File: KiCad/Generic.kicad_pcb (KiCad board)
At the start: 2 copper layers, 19 x 29 mm, 16 parts, among them J1 Connector, J2 USB-C, J3 VBUS, M1 D24V5F3-NoSHDN, U1 ESP32-WROOM-32, U2 FT231XQ

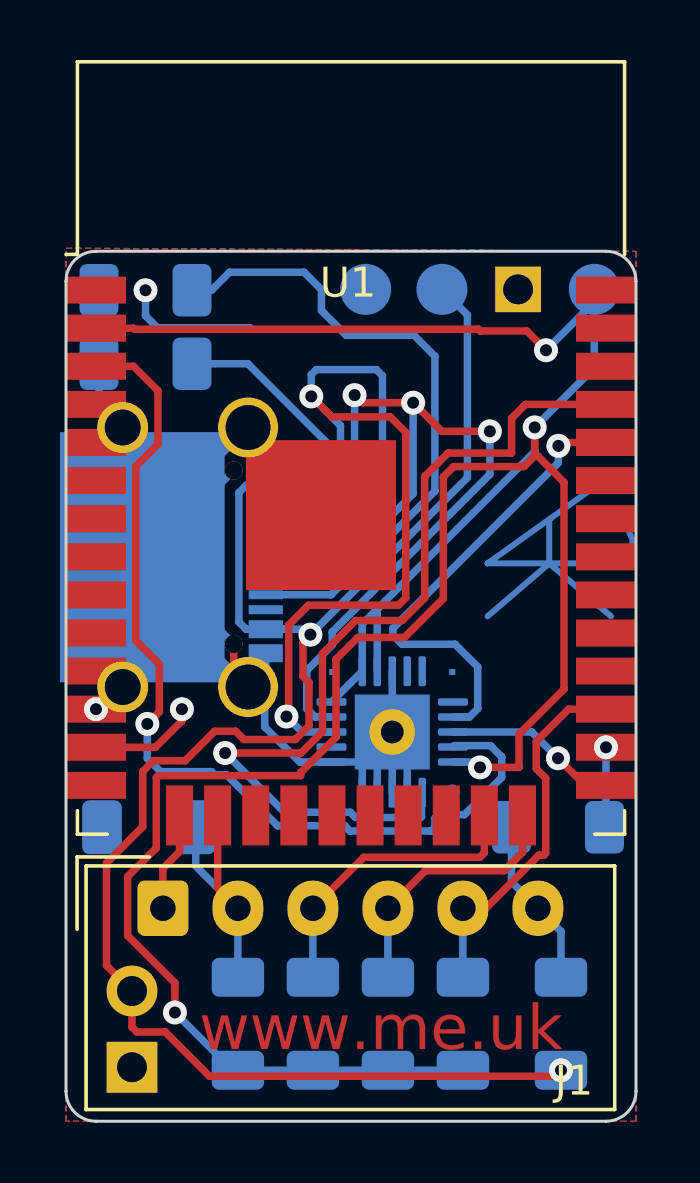
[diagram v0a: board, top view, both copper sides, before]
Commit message: New regulator
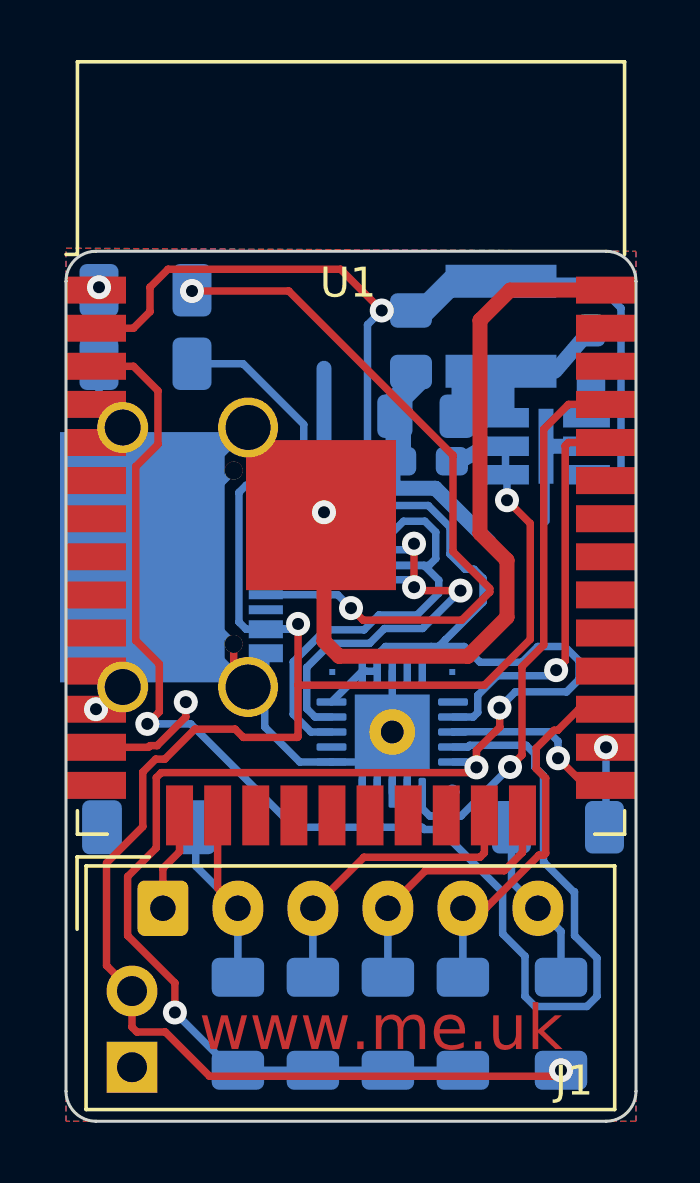
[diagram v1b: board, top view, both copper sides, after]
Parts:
- removed AJK1: AJK, RevK:AJK
- removed M1: D24V5F3-NoSHDN, RevK:D24V5F3-SMD-Like
- added Reg1: Regulator, RevK:RegulatorBlock, B.Cu at (126.0, 107.5)
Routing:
- net GND: track 70.5 -> 105.1 mm, vias 2 -> 3
- net +3V3: track 92.5 -> 77.3 mm
- net EN: track 31.7 -> 46.8 mm
- net D+: track 37.5 -> 23.9 mm, vias 2 -> 0
- net D-: track 34.3 -> 21.6 mm
- net O: track 30.3 -> 18.4 mm
- net Net-(J2-PadA5): track 21.5 -> 24.2 mm, vias 0 -> 2
- net VBUS: track 56.8 -> 59.6 mm, vias 2 -> 3
- net I: track 15.8 -> 13.4 mm
- net Net-(J2-PadB5): track 9.51 -> 8.24 mm

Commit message: Regulator
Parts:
- R7, R8: footprint Resistor_SMD:R_1206_3216Metric_Pad1.30x1.75mm_HandSolder -> Resistor_SMD:R_0603_1608Metric_Pad0.98x0.95mm_HandSolder
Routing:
- net +3V3: track 77.3 -> 79.7 mm
- net GND: track 105.1 -> 104.2 mm
- net Net-(J2-PadA5): track 24.2 -> 24.9 mm
- net Net-(J2-PadB5): track 8.24 -> 8.88 mm

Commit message: Reg
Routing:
- net +3V3: track 79.7 -> 73.8 mm
- net GND: track 104.2 -> 100.6 mm
- net VBUS: track 59.6 -> 57.6 mm
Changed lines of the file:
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@@
     (thickness 1.6)
     (drawings 13)
-    (tracks 355)
+    (tracks 334)
     (zones 0)
     (modules 15)
@@
     (fp_line (start 0.5 2.5) (end 0.5 3) (layer B.Cu) (width 0.25))
     (fp_line (start 0.5 2.5) (end -0.95 2.5) (layer B.Cu) (width 0.25))
+    (pad 4 smd rect (at 4.8 -0.7) (size 0.5 1) (layers B.Cu)
+      (net 4 +3V3) (zone_connect 0))
+    (pad 4 smd roundrect (at 3.95 -4.3 315) (size 0.5 0.5) (layers B.Cu) (roundrect_rratio 0.25)
+      (net 4 +3V3) (zone_connect 0))
+    (pad 4 smd roundrect (at 4 -4.15 90) (size 0.5 0.5) (layers B.Cu) (roundrect_rratio 0.25)
+      (net 4 +3V3) (zone_connect 0))
+    (pad 4 smd rect (at 3.7 -4.55 315) (size 0.5 1) (layers B.Cu)
+      (net 4 +3V3) (zone_connect 0))
+    (pad 2 smd roundrect (at 0 -2.2 90) (size 0.5 0.5) (layers B.Cu) (roundrect_rratio 0.25)
+      (net 5 VBUS) (zone_connect 0))
+    (pad 2 smd roundrect (at -0.05 -2.35 315) (size 0.5 0.5) (layers B.Cu) (roundrect_rratio 0.25)
+      (net 5 VBUS) (zone_connect 0))
+    (pad 2 smd rect (at 0 -1.85 90) (size 0.5 1) (layers B.Cu)
+      (net 5 VBUS) (zone_connect 0))
+    (pad 2 smd rect (at -0.35 -2.65 315) (size 0.5 1) (layers B.Cu)
+      (net 5 VBUS) (zone_connect 0))
+    (pad 3 smd rect (at 5.25 -4.35 90) (size 0.5 1) (layers B.Cu)
+      (net 2 GND) (zone_connect 0))
+    (pad 3 smd rect (at 5.25 -3.5 90) (size 0.5 1) (layers B.Cu)
+      (net 2 GND) (zone_connect 0))
+    (pad 3 smd rect (at 0 0.75 90) (size 0.5 1) (layers B.Cu)
+      (net 2 GND) (zone_connect 0))
+    (pad 3 smd rect (at 0 0.15 90) (size 0.5 0.8) (layers B.Cu)
+      (net 2 GND) (zone_connect 0))
     (pad 3 smd rect (at 5.25 -4 90) (size 0.5 1) (layers B.Cu)
       (net 2 GND) (zone_connect 0))
-    (pad 4 smd rect (at 4.1 -0.81 135) (size 0.5 0.5) (layers B.Cu)
+    (pad 4 smd roundrect (at 4 -0.7 90) (size 0.5 0.5) (layers B.Cu) (roundrect_rratio 0.25)
       (net 4 +3V3) (zone_connect 0))
-    (pad 4 smd rect (at 4.6 -0.71) (size 0.5 1) (layers B.Cu)
+    (pad 4 smd rect (at 4.4 -0.7) (size 0.5 1) (layers B.Cu)
       (net 4 +3V3) (zone_connect 0))
-    (pad 4 smd rect (at 4 -2.56 90) (size 0.5 3.5) (layers B.Cu)
+    (pad 4 smd rect (at 4 -2.4 90) (size 0.5 3.65) (layers B.Cu)
       (net 4 +3V3) (zone_connect 0))
-    (pad 4 smd rect (at 3.72 -4.48 135) (size 0.5 1) (layers B.Cu)
-      (net 4 +3V3) (zone_connect 0))
-    (pad 2 smd rect (at -0.25 -2.5 110) (size 0.5 1) (layers B.Cu)
-      (net 5 VBUS) (zone_connect 0))
     (pad ~ smd roundrect (at 2.2625 -2.75 90) (size 1.425 1.75) (layers B.Cu B.Paste B.Mask) (roundrect_rratio 0.175))
     (pad 3 smd roundrect (at 5.2375 -2.75 90) (size 1.425 1.75) (layers B.Cu B.Paste B.Mask) (roundrect_rratio 0.175)
@@
     (pad 3 smd rect (at 0 0) (size 0.5 2.5) (layers B.Cu)
       (net 2 GND))
-    (pad 3 smd rect (at 0 0.4 90) (size 0.5 1) (layers B.Cu)
+    (pad 3 smd rect (at 0 0.4 90) (size 0.5 0.8) (layers B.Cu)
       (net 2 GND) (zone_connect 0))
     (pad 4 smd rect (at 5.25 0.25) (size 3.7 1.1) (layers B.Cu B.Paste B.Mask)
@@
   (segment (start 119.1 114.5) (end 118.6 114) (width 0.5) (layer F.Cu) (net 2))
   (segment (start 123.4 114.5) (end 119.1 114.5) (width 0.5) (layer F.Cu) (net 2))
-  (segment (start 121.975 102.225) (end 122 102.25) (width 0.25) (layer B.Cu) (net 2))
-  (segment (start 121 102.225) (end 121.975 102.225) (width 0.25) (layer B.Cu) (net 2))
-  (segment (start 123.2375 102.25) (end 123.25 102.2625) (width 0.25) (layer B.Cu) (net 2))
-  (segment (start 122 102.25) (end 123.2375 102.25) (width 0.25) (layer B.Cu) (net 2))
-  (segment (start 126.4 107.5) (end 126 107.5) (width 0.25) (layer B.Cu) (net 2))
-  (segment (start 127.35 107.5) (end 126.4 107.5) (width 0.25) (layer B.Cu) (net 2))
   (segment (start 121 102.225) (end 118.625 102.225) (width 0.25) (layer B.Cu) (net 2))
   (segment (start 121.1375 108.5375) (end 121.5 108.9) (width 0.5) (layer B.Cu) (net 2))
@@
   (segment (start 123.27499 114.17499) (end 123.8 114.7) (width 0.25) (layer B.Cu) (net 4))
   (segment (start 126.25 102.25) (end 125.45 102.25) (width 0.25) (layer B.Cu) (net 4))
-  (segment (start 125.29 102.41) (end 125.29 102.9) (width 0.25) (layer B.Cu) (net 4))
-  (segment (start 125.45 102.25) (end 125.29 102.41) (width 0.25) (layer B.Cu) (net 4))
-  (segment (start 125.29 103.3) (end 125.19 103.4) (width 0.25) (layer B.Cu) (net 4))
-  (segment (start 125.29 102.9) (end 125.29 103.3) (width 0.25) (layer B.Cu) (net 4))
-  (segment (start 125.09 103.5) (end 125.19 103.4) (width 0.25) (layer B.Cu) (net 4))
-  (segment (start 123.44 103.5) (end 125.09 103.5) (width 0.25) (layer B.Cu) (net 4))
-  (segment (start 121.8 103.5) (end 121.52 103.78) (width 0.25) (layer B.Cu) (net 4))
-  (segment (start 123.44 103.5) (end 121.8 103.5) (width 0.25) (layer B.Cu) (net 4))
-  (segment (start 121.025 104.275) (end 121.52 103.78) (width 0.25) (layer B.Cu) (net 4))
-  (segment (start 121 104.275) (end 121.025 104.275) (width 0.25) (layer B.Cu) (net 4))
   (segment (start 120.62499 109.47501) (end 120.04999 108.90001) (width 0.25) (layer B.Cu) (net 4))
   (segment (start 120.04999 108.90001) (end 120.04999 105.22501) (width 0.25) (layer B.Cu) (net 4))
@@
   (segment (start 122.422718 114.17499) (end 123.899977 112.697731) (width 0.25) (layer B.Cu) (net 4))
   (via (at 119.8 104.2) (size 0.8) (drill 0.4) (layers F.Cu B.Cu) (net 4))
-  (segment (start 120.925 104.2) (end 121 104.275) (width 0.25) (layer B.Cu) (net 4))
   (segment (start 119.8 104.2) (end 120.925 104.2) (width 0.25) (layer B.Cu) (net 4))
   (segment (start 119.8 104.97502) (end 120.04999 105.22501) (width 0.25) (layer B.Cu) (net 4))
@@
   (segment (start 125.475011 110.075011) (end 124.7 109.3) (width 0.25) (layer F.Cu) (net 5))
   (segment (start 125.475011 113.938177) (end 125.475011 110.075011) (width 0.25) (layer F.Cu) (net 5))
-  (segment (start 123.25 108) (end 123.5 107.75) (width 0.25) (layer B.Cu) (net 5))
-  (segment (start 122.8625 108) (end 123.25 108) (width 0.25) (layer B.Cu) (net 5))
-  (segment (start 123.75 107.5) (end 123.5 107.75) (width 0.25) (layer B.Cu) (net 5))
-  (segment (start 124.65 107.5) (end 123.75 107.5) (width 0.25) (layer B.Cu) (net 5))
   (segment (start 124.65 107.5) (end 124.65 108.45) (width 0.25) (layer B.Cu) (net 5))
   (segment (start 124.7 108.5) (end 124.65 108.45) (width 0.25) (layer B.Cu) (net 5))

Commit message: Footprint tidy
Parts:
- added C2: 100nF, Capacitor_SMD:C_0603_1608Metric_Pad1.08x0.95mm_HandSolder, B.Cu at (125.0, 112.0)
- J1: footprint Connector_Molex:Molex_SPOX_5268-06A_1x06_P2.50mm_Horizontal -> RevK:Molex_MiniSPOX_H6RA
- moved J1 6.25 mm to (119.5, 122.9)
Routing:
- net GND: track 100.6 -> 82.4 mm
- net +3V3: track 73.8 -> 74.9 mm

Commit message: Tidy up
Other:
- board text added: "13"
- board text added: "15"
- board text added: "16"
- board text added: "2"
- board text added: "4"
- board text added: "Ext Power"
- board text added: "GND"
- board text added: "Link to 3.3V"
- board text added: "Link to 5V"
- board text added: "Link to GND for pin 2"
- board text added: "Series link for pin 6"
